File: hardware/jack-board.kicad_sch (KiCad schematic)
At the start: 13 parts, among them J1 AudioJack2_SwitchT, J10 AudioJack2_SwitchT, J11 AudioJack2_SwitchT, J2 AudioJack2_SwitchT, J3 AudioJack2_SwitchT, J4 AudioJack2_SwitchT, J5 AudioJack2_SwitchT, J6 AudioJack2_SwitchT, J8 AudioJack2_SwitchT, J9 AudioJack2_SwitchT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

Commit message: Fix 3d models and migrate to KiCad6 R/C footprints
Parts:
- R16, R24: footprint Resistor_SMD:R_0603_1608Metric_Pad1.05x0.95mm_HandSolder -> Resistor_SMD:R_0603_1608Metric_Pad0.98x0.95mm_HandSolder
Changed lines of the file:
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@@
       (effects (font (size 1.27 1.27)) (justify left))
     )
-    (property "Footprint" "Resistor_SMD:R_0603_1608Metric_Pad1.05x0.95mm_HandSolder" (id 2) (at 68.834 108.966 90)
+    (property "Footprint" "Resistor_SMD:R_0603_1608Metric_Pad0.98x0.95mm_HandSolder" (id 2) (at 68.834 108.966 90)
       (effects (font (size 1.27 1.27)) hide)
     )
@@
     (property "Reference" "R24" (id 0) (at 107.823 66.04 90))
     (property "Value" "51" (id 1) (at 110.1344 66.04 90))
-    (property "Footprint" "Resistor_SMD:R_0603_1608Metric_Pad1.05x0.95mm_HandSolder" (id 2) (at 112.014 65.786 90)
+    (property "Footprint" "Resistor_SMD:R_0603_1608Metric_Pad0.98x0.95mm_HandSolder" (id 2) (at 112.014 65.786 90)
       (effects (font (size 1.27 1.27)) hide)
     )

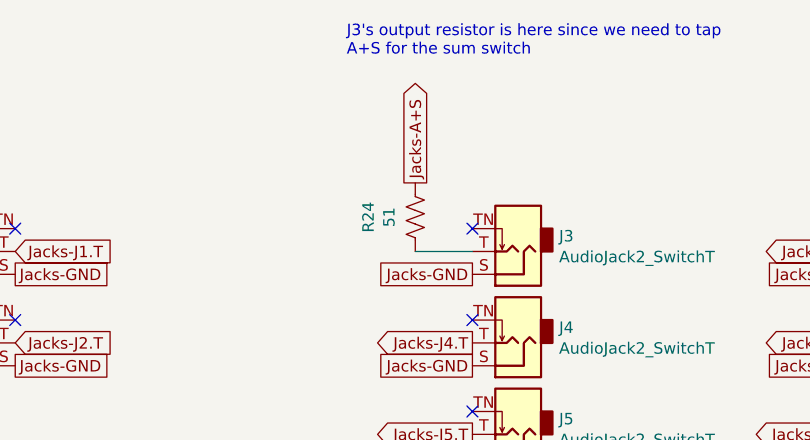
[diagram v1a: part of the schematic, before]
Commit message: Redesign output circuits
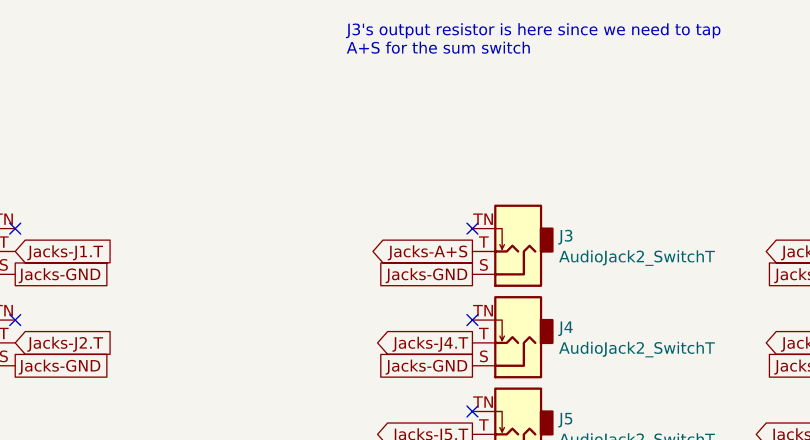
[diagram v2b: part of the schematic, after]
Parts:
- removed R24: 51, Resistor_SMD:R_0603_1608Metric_Pad0.98x0.95mm_HandSolder, symbol Device:R_US
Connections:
- net Jacks-A+S: now also J3.T
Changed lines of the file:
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@@
-    (stroke (width 0) (type default) (color 0 0 0 0))
-  )
-  (wire (pts (xy 113.03 69.85) (xy 119.38 69.85))
     (stroke (width 0) (type default) (color 0 0 0 0))
   )
@@
     )
   )
-  (global_label "Jacks-A+S" (shape output) (at 113.03 62.23 90) (fields_autoplaced)
-    (effects (font (size 1.27 1.27)) (justify left))
-    (property "Intersheet References" "${INTERSHEET_REFS}" (id 0) (at 0 0 0)
+  (global_label "Jacks-A+S" (shape output) (at 119.38 69.85 180) (fields_autoplaced)
+    (effects (font (size 1.27 1.27)) (justify right))
+    (property "Intersheet References" "${INTERSHEET_REFS}" (id 0) (at 57.15 182.88 0)
       (effects (font (size 1.27 1.27)) hide)
     )
@@
     (pin "3")
   )
-  (symbol (lib_id "Device:R_US") (at 113.03 66.04 180) (unit 1)
-    (in_bom yes) (on_board yes)
-    (property "Reference" "R24" (id 0) (at 107.823 66.04 90))
-    (property "Value" "51" (id 1) (at 110.1344 66.04 90))
-    (property "Footprint" "Resistor_SMD:R_0603_1608Metric_Pad0.98x0.95mm_HandSolder" (id 2) (at 112.014 65.786 90)
-      (effects (font (size 1.27 1.27)) hide)
-    )
-    (property "Datasheet" "~" (id 3) (at 113.03 66.04 0)
-      (effects (font (size 1.27 1.27)) hide)
-    )
-    (property "Tolerance" "5%" (id 4) (at 113.03 66.04 0)
-      (effects (font (size 1.27 1.27)) hide)
-    )
-    (pin "1")
-    (pin "2")
-  )
 )
